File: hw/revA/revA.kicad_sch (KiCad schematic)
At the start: 10 parts, among them U1 CY7C68013A-56LTX, U2 CY7C68013A-56LTX, U3 W25Q128JVS, Y1 Crystal

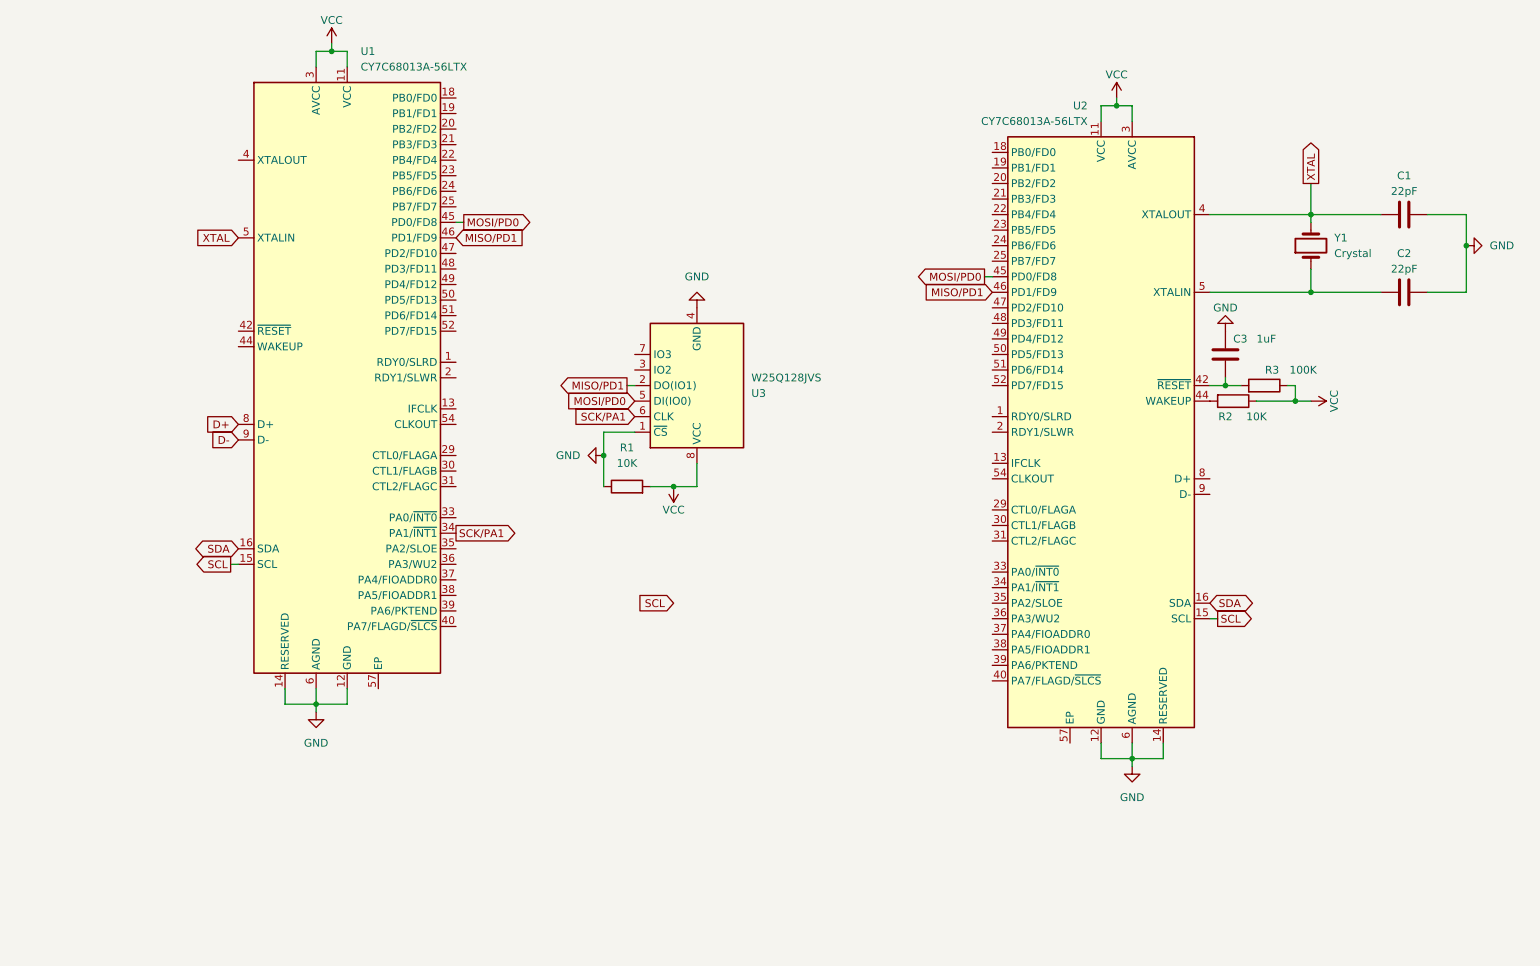
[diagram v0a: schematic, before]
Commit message: hw: Finish rough board schematic (except for FIFOs)
These schematics are subject to change, but this is the gist of what I
am trying to do here.  I have a pretty good idea of the form factor I'm
shooting for, and I know what footprints I want for the big-ticket items
already (for the most part).  I am operating under the assumption that I
can share a single EEPROM chip between the two FX2 devices, since only
one of them should ever be loading the USB IDs and bootloader from the
I²C EEPROM on the bus at a time.

The only thing left to do now is figure out how I'm wiring up my
hardware FIFOs between the two FX2 devices.
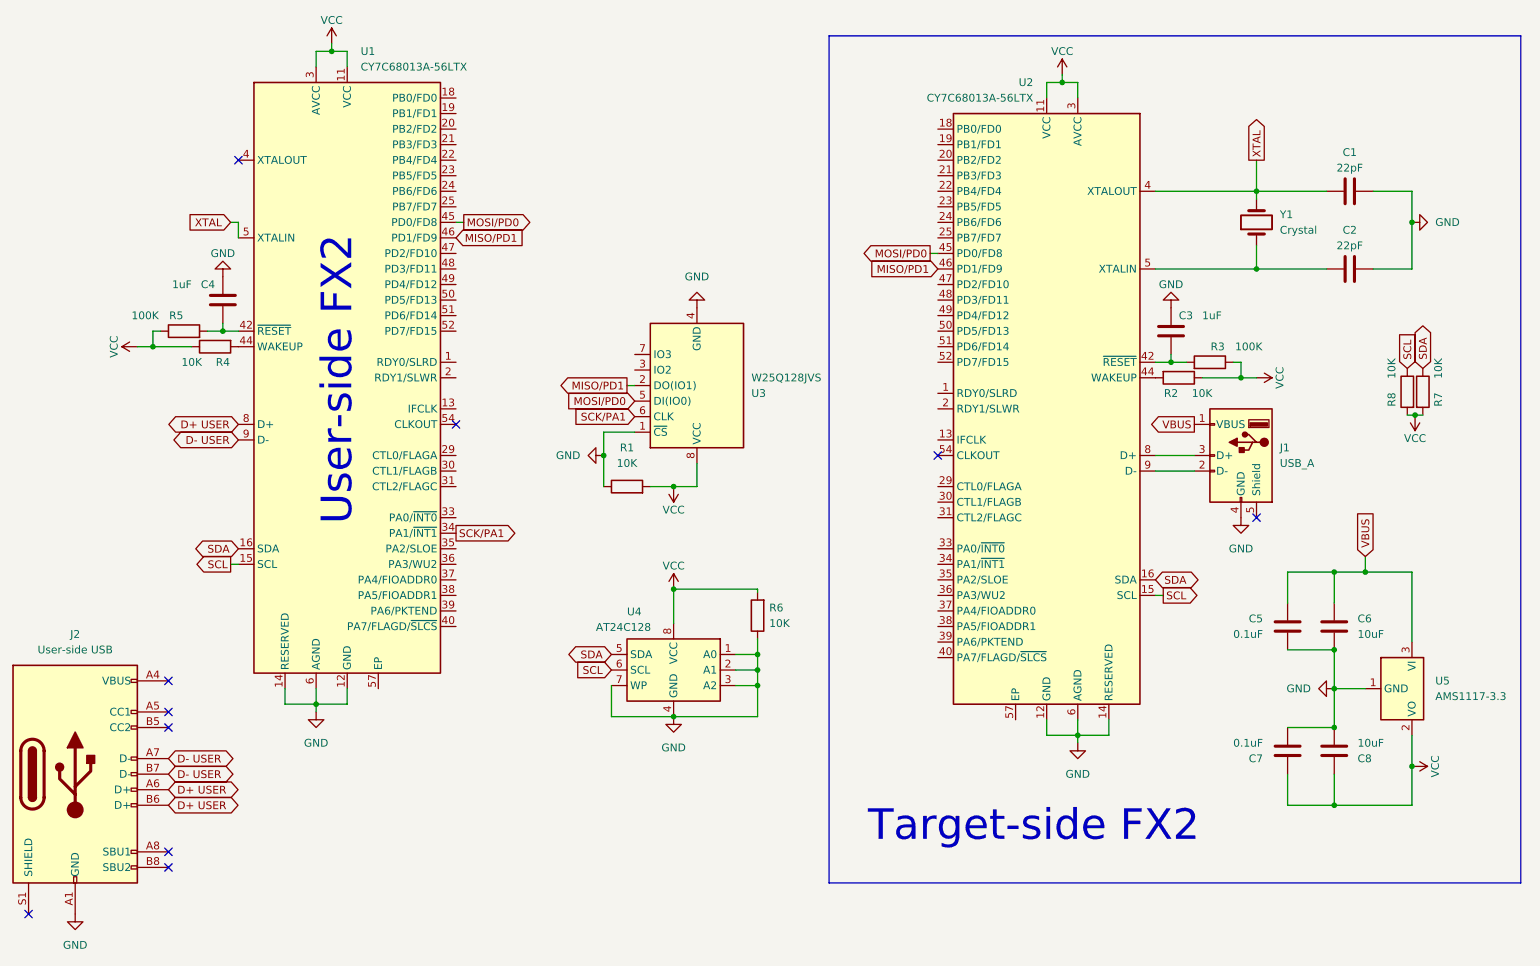
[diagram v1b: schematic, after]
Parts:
- added C4: 1uF, symbol Device:C
- added C5, C7: 0.1uF, symbol Device:C
- added C6, C8: 10uF, symbol Device:C
- added J1: USB_A, symbol Connector:USB_A
- added J2: User-side USB, symbol Connector:USB_C_Receptacle_USB2.0
- added R4, R6, R7, R8: 10K, symbol Device:R
- added R5: 100K, symbol Device:R
- added U4: AT24C128, symbol Memory_EEPROM:CAT24C128
- added U5: AMS1117-3.3, Package_TO_SOT_SMD:SOT-223-3_TabPin2, symbol Regulator_Linear:AMS1117-3.3
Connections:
- net GND: now also C4.1, C5.1, C6.1, C7.1, C8.1, J1.4 (GND), J2.A1 (GND), J2.A12 (GND), J2.B1 (GND), J2.B12 (GND), R6.1, U4.1 (A0), U4.2 (A1), U4.3 (A2), U4.4 (GND), U4.7 (WP), U5.1 (GND)
- net SCL: now also R8.1, U4.6 (SCL)
- net SDA: now also R7.1, U4.5 (SDA)
- net VCC: now also C7.2, C8.2, R4.1, R5.1, R6.2, R7.2, R8.2, U4.8 (VCC), U5.2 (VO)
- net at U1.42 (~{RESET}): now also C4.2, R5.2
- net at U1.44 (WAKEUP): now also R4.2
- net at U2.8 (D+): now also J1.3 (D+)
- net at U2.9 (D-): now also J1.2 (D-)
- net D+ renamed D+ USER
- net D+ USER: now also J2.A6 (D+), J2.B6 (D+)
- net D- renamed D- USER
- net D- USER: now also J2.A7 (D-), J2.B7 (D-)
- new net: J2.A4 (VBUS), J2.A9 (VBUS), J2.B4 (VBUS), J2.B9 (VBUS)
- new net VBUS: C5.2, C6.2, J1.1 (VBUS), U5.3 (VI)
- no-connect marks 0 -> 10
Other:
- note added: "Target-side FX2"
- note added: "User-side FX2"
- moved on the sheet: C1, C2, C3, R2, R3, U2, Y1

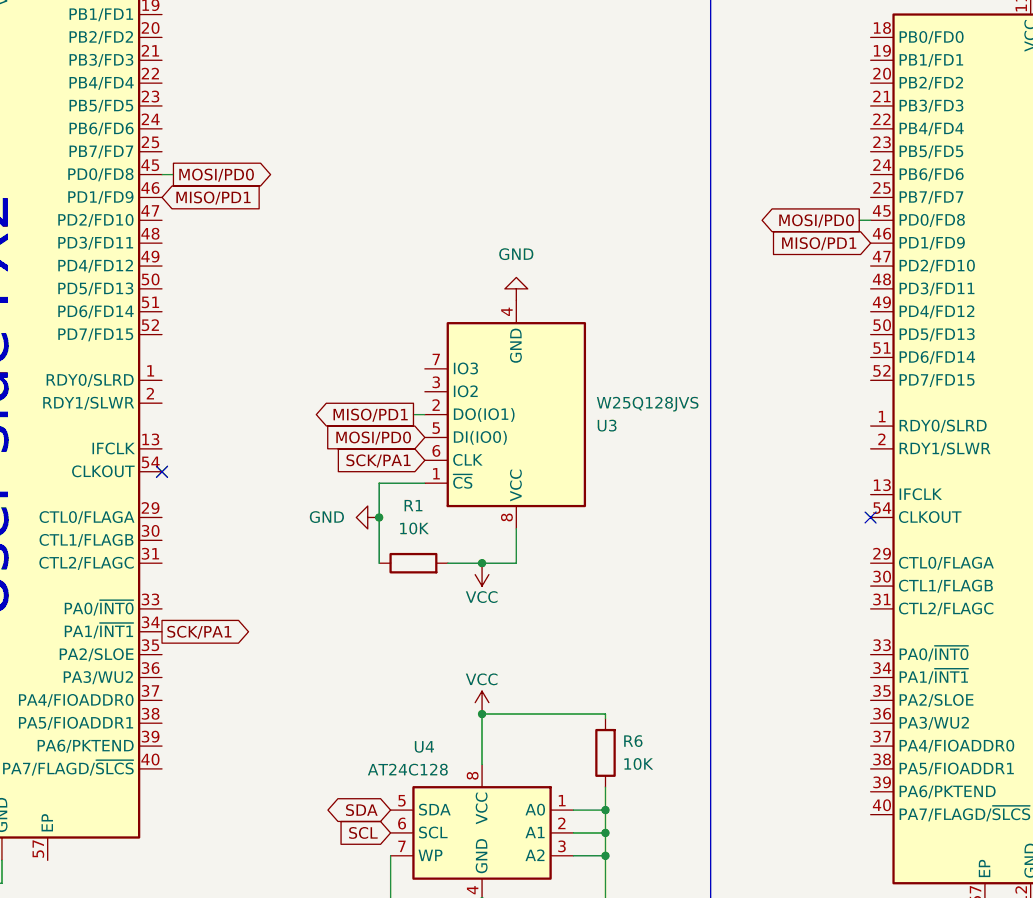
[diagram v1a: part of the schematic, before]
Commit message: hw: Move all SPI to port A
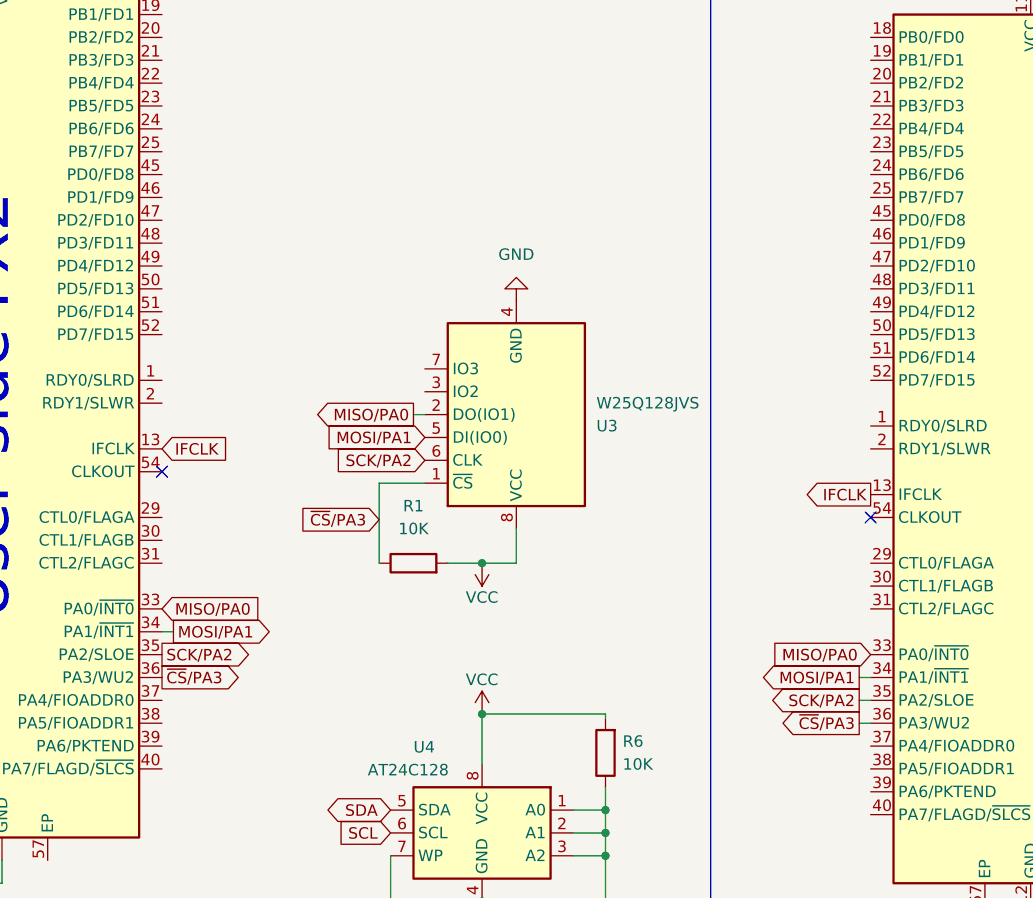
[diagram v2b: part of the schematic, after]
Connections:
- net GND: no longer R1.1, U3.1 (~{CS})
- net IFCLK: now reaches U1.13 (IFCLK)
- net IFCLK: now also U2.13 (IFCLK)
- net MISO/PA0: now reaches U1.33 (PA0/~{INT0})
- net MISO/PA0: now also U2.33 (PA0/~{INT0}), U3.2 (DO(IO1))
- net SCK/PA2: now reaches U1.35 (PA2/SLOE)
- net SCK/PA2: now also U2.35 (PA2/SLOE), U3.6 (CLK)
- net ~{CS}/PA3: now reaches U1.36 (PA3/WU2)
- net ~{CS}/PA3: now also R1.1, U2.36 (PA3/WU2), U3.1 (~{CS})
- net MOSI/PA1: now reaches U2.34 (PA1/~{INT1})
- net MOSI/PA1: now also U1.34 (PA1/~{INT1}), U3.5 (DI(IO0))
- removed net MISO/PD1: U1.46 (PD1/FD9), U2.46 (PD1/FD9), U3.2 (DO(IO1))
- removed net MOSI/PD0: U1.45 (PD0/FD8), U2.45 (PD0/FD8), U3.5 (DI(IO0))
- removed net SCK/PA1: U1.34 (PA1/~{INT1}), U3.6 (CLK)
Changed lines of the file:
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@@
   (junction (at 246.38 104.14) (diameter 0) (color 0 0 0 0)
-  )
-  (junction (at 121.92 85.09) (diameter 0) (color 0 0 0 0)
   )
   (junction (at 226.06 72.39) (diameter 0) (color 0 0 0 0)
@@
     (stroke (width 0) (type default))
   )
-  (wire (pts (xy 121.92 85.09) (xy 121.92 81.28))
-    (stroke (width 0) (type default))
-  )
   (wire (pts (xy 62.23 46.99) (xy 62.23 49.53))
     (stroke (width 0) (type default))
@@
     (stroke (width 0) (type default))
   )
-  (wire (pts (xy 176.53 52.07) (xy 175.26 52.07))
-    (stroke (width 0) (type default))
-  )
   (wire (pts (xy 74.93 125.73) (xy 74.93 127))
     (stroke (width 0) (type default))
   )
+  (wire (pts (xy 176.53 102.87) (xy 175.26 102.87))
+    (stroke (width 0) (type default))
+  )
   (wire (pts (xy 228.6 54.61) (xy 212.09 54.61))
     (stroke (width 0) (type default))
@@
     (stroke (width 0) (type default))
   )
-  (wire (pts (xy 121.92 90.17) (xy 121.92 85.09))
+  (wire (pts (xy 121.92 81.28) (xy 121.92 90.17))
     (stroke (width 0) (type default))
   )
@@
     (stroke (width 0) (type default))
   )
+  (wire (pts (xy 175.26 105.41) (xy 176.53 105.41))
+    (stroke (width 0) (type default))
+  )
   (wire (pts (xy 62.23 64.77) (xy 59.69 64.77))
     (stroke (width 0) (type default))
@@
     (stroke (width 0) (type default))
   )
+  (wire (pts (xy 175.26 107.95) (xy 176.53 107.95))
+    (stroke (width 0) (type default))
+  )
   (wire (pts (xy 196.85 24.13) (xy 194.31 24.13))
     (stroke (width 0) (type default))
@@
     (stroke (width 0) (type default))
   )
-  (wire (pts (xy 97.79 46.99) (xy 99.06 46.99))
+  (wire (pts (xy 97.79 97.79) (xy 99.06 97.79))
     (stroke (width 0) (type default))
   )
@@
     (effects (font (size 5 5)) (justify left bottom))
   )
+  (global_label "IFCLK" (shape input) (at 97.79 77.47 0) (fields_autoplaced)
+    (effects (font (size 1.27 1.27)) (justify left))
+    (property "Intersheetrefs" "${INTERSHEET_REFS}" (at 106.0367 77.47 0)
+      (effects (font (size 1.27 1.27)) (justify left) hide)
+    )
+  )
   (global_label "SCL" (shape output) (at 60.96 102.87 180) (fields_autoplaced)
     (effects (font (size 1.27 1.27)) (justify right))
@@
     )
   )
-  (global_label "MISO{slash}PD1" (shape output) (at 125.73 73.66 180) (fields_autoplaced)
+  (global_label "MISO{slash}PA0" (shape output) (at 125.73 73.66 180) (fields_autoplaced)
     (effects (font (size 1.27 1.27)) (justify right))
     (property "Intersheetrefs" "${INTERSHEET_REFS}" (at 113.0686 73.66 0)
@@
     )
   )
+  (global_label "MOSI{slash}PA1" (shape output) (at 175.26 102.87 180) (fields_autoplaced)
+    (effects (font (size 1.27 1.27)) (justify right))
+    (property "Intersheetrefs" "${INTERSHEET_REFS}" (at 162.5986 102.87 0)
+      (effects (font (size 1.27 1.27)) (justify right) hide)
+    )
+  )
+  (global_label "MISO{slash}PA0" (shape input) (at 176.53 100.33 180) (fields_autoplaced)
+    (effects (font (size 1.27 1.27)) (justify right))
+    (property "Intersheetrefs" "${INTERSHEET_REFS}" (at 163.8686 100.33 0)
+      (effects (font (size 1.27 1.27)) (justify right) hide)
+    )
+  )
   (global_label "D- USER" (shape bidirectional) (at 50.8 134.62 0) (fields_autoplaced)
     (effects (font (size 1.27 1.27)) (justify left))
@@
     )
   )
-  (global_label "MISO{slash}PD1" (shape input) (at 176.53 54.61 180) (fields_autoplaced)
-    (effects (font (size 1.27 1.27)) (justify right))
-    (property "Intersheetrefs" "${INTERSHEET_REFS}" (at 163.8686 54.61 0)
-      (effects (font (size 1.27 1.27)) (justify right) hide)
-    )
-  )
-  (global_label "SCK{slash}PA1" (shape input) (at 127 78.74 180) (fields_autoplaced)
+  (global_label "SCK{slash}PA2" (shape input) (at 127 78.74 180) (fields_autoplaced)
     (effects (font (size 1.27 1.27)) (justify right))
     (property "Intersheetrefs" "${INTERSHEET_REFS}" (at 115.3667 78.74 0)
@@
     )
   )
-  (global_label "MISO{slash}PD1" (shape input) (at 97.79 49.53 0) (fields_autoplaced)
-    (effects (font (size 1.27 1.27)) (justify left))
-    (property "Intersheetrefs" "${INTERSHEET_REFS}" (at 110.4514 49.53 0)
+  (global_label "MISO{slash}PA0" (shape input) (at 97.79 95.25 0) (fields_autoplaced)
+    (effects (font (size 1.27 1.27)) (justify left))
+    (property "Intersheetrefs" "${INTERSHEET_REFS}" (at 110.4514 95.25 0)
       (effects (font (size 1.27 1.27)) (justify left) hide)
     )
@@
     )
   )
-  (global_label "MOSI{slash}PD0" (shape output) (at 99.06 46.99 0) (fields_autoplaced)
-    (effects (font (size 1.27 1.27)) (justify left))
-    (property "Intersheetrefs" "${INTERSHEET_REFS}" (at 111.7214 46.99 0)
-      (effects (font (size 1.27 1.27)) (justify left) hide)
-    )
-  )
-  (global_label "MOSI{slash}PD0" (shape output) (at 175.26 52.07 180) (fields_autoplaced)
-    (effects (font (size 1.27 1.27)) (justify right))
-    (property "Intersheetrefs" "${INTERSHEET_REFS}" (at 162.5986 52.07 0)
-      (effects (font (size 1.27 1.27)) (justify right) hide)
-    )
-  )
-  (global_label "MOSI{slash}PD0" (shape input) (at 127 76.2 180) (fields_autoplaced)
+  (global_label "MOSI{slash}PA1" (shape output) (at 99.06 97.79 0) (fields_autoplaced)
+    (effects (font (size 1.27 1.27)) (justify left))
+    (property "Intersheetrefs" "${INTERSHEET_REFS}" (at 111.7214 97.79 0)
+      (effects (font (size 1.27 1.27)) (justify left) hide)
+    )
+  )
+  (global_label "MOSI{slash}PA1" (shape input) (at 127 76.2 180) (fields_autoplaced)
     (effects (font (size 1.27 1.27)) (justify right))
     (property "Intersheetrefs" "${INTERSHEET_REFS}" (at 114.3386 76.2 0)
@@
     )
   )
+  (global_label "~{CS}{slash}PA3" (shape input) (at 121.92 85.344 180) (fields_autoplaced)
+    (effects (font (size 1.27 1.27)) (justify right))
+    (property "Intersheetrefs" "${INTERSHEET_REFS}" (at 111.5567 85.344 0)
+      (effects (font (size 1.27 1.27)) (justify right) hide)
+    )
+  )
   (global_label "VBUS" (shape output) (at 218.44 80.01 180) (fields_autoplaced)
     (effects (font (size 1.27 1.27)) (justify right))
@@
     )
   )
+  (global_label "SCK{slash}PA2" (shape output) (at 175.26 105.41 180) (fields_autoplaced)
+    (effects (font (size 1.27 1.27)) (justify right))
+    (property "Intersheetrefs" "${INTERSHEET_REFS}" (at 163.6267 105.41 0)
+      (effects (font (size 1.27 1.27)) (justify right) hide)
+    )
+  )
   (global_label "D- USER" (shape bidirectional) (at 50.8 137.16 0) (fields_autoplaced)
     (effects (font (size 1.27 1.27)) (justify left))
@@
     )
   )
-  (global_label "SCK{slash}PA1" (shape output) (at 97.79 97.79 0) (fields_autoplaced)
-    (effects (font (size 1.27 1.27)) (justify left))
-    (property "Intersheetrefs" "${INTERSHEET_REFS}" (at 109.4233 97.79 0)
+  (global_label "IFCLK" (shape output) (at 176.53 82.55 180) (fields_autoplaced)
+    (effects (font (size 1.27 1.27)) (justify right))
+    (property "Intersheetrefs" "${INTERSHEET_REFS}" (at 168.2833 82.55 0)
+      (effects (font (size 1.27 1.27)) (justify right) hide)
+    )
+  )
+  (global_label "~{CS}{slash}PA3" (shape output) (at 97.79 102.87 0) (fields_autoplaced)
+    (effects (font (size 1.27 1.27)) (justify left))
+    (property "Intersheetrefs" "${INTERSHEET_REFS}" (at 108.1533 102.87 0)
+      (effects (font (size 1.27 1.27)) (justify left) hide)
+    )
+  )
+  (global_label "SCK{slash}PA2" (shape output) (at 97.79 100.33 0) (fields_autoplaced)
+    (effects (font (size 1.27 1.27)) (justify left))
+    (property "Intersheetrefs" "${INTERSHEET_REFS}" (at 109.4233 100.33 0)
       (effects (font (size 1.27 1.27)) (justify left) hide)
     )
@@
     (property "Intersheetrefs" "${INTERSHEET_REFS}" (at 219.8528 107.95 0)
       (effects (font (size 1.27 1.27)) (justify left) hide)
+    )
+  )
+  (global_label "~{CS}{slash}PA3" (shape output) (at 175.26 107.95 180) (fields_autoplaced)
+    (effects (font (size 1.27 1.27)) (justify right))
+    (property "Intersheetrefs" "${INTERSHEET_REFS}" (at 164.8967 107.95 0)
+      (effects (font (size 1.27 1.27)) (justify right) hide)
     )
   )
@@
         )
       )
-    )
-  )
-  (symbol (lib_id "power:GND") (at 121.92 85.09 270) (unit 1)
-    (in_bom yes) (on_board yes) (dnp no) (fields_autoplaced)
-    (property "Reference" "#PWR07" (at 115.57 85.09 0)
-      (effects (font (size 1.27 1.27)) hide)
-    )
-    (property "Value" "GND" (at 118.11 85.09 90)
-      (effects (font (size 1.27 1.27)) (justify right))
-    )
-    (property "Footprint" "" (at 121.92 85.09 0)
-      (effects (font (size 1.27 1.27)) hide)
-    )
-    (property "Datasheet" "" (at 121.92 85.09 0)
-      (effects (font (size 1.27 1.27)) hide)
-    )
-    (pin "1")
-    (instances
-      (project "revA"
-        (path "/6b879416-04f6-44b0-8781-f2884cc38922"
-          (reference "#PWR07") (unit 1)
-        )
-      )
